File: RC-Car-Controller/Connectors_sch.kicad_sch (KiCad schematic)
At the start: 6 parts, among them J1 MCU_IF, J3 MOTOR_IF, J4 BATT_1, J5 MISC_IF, J6 ANT_IF, J7 BATT2

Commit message: Fixed Controller PCB
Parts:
- removed J3: MOTOR_IF, symbol Connector:Conn_01x06_Pin
- removed J4: BATT_1, footprints:CONN_1805375_RSP, symbol Connector:Conn_01x02_Pin
- removed J5: MISC_IF, symbol Connector:Conn_01x06_Pin
- removed J7: BATT2, footprints:CONN_1805375_RSP, symbol Connector:Conn_01x02_Pin
- added J1, J2: XT60-M, symbol XT60-M:XT60-M
- renumbered J1 to J5
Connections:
- net GND_BATT: now also J1.N (NEG), J2.N (NEG)
- net VDD_BATT: now also J1.P (POS), J2.P (POS)
- no-connect marks 7 -> 1
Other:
- note added: "Battery CON"
- moved on the sheet: J5

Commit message: Did some stuff on the Controller
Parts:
- removed J1, J2: XT60-M, symbol XT60-M:XT60-M
- added J1, J4: Conn_01x02, Connector_JST:JST_XH_B2B-XH-AM_1x02_P2.50mm_Vertical, symbol Connector_Generic:Conn_01x02
- added J2: USB_C_Receptacle_USB2.0_16P, symbol Connector:USB_C_Receptacle_USB2.0_16P
- added R18: 1Mohm, Resistor_SMD:R_0603_1608Metric, symbol Device:R
- added R19, R20: 5.11kohm, Resistor_SMD:R_0603_1608Metric, symbol Device:R
- added U2: USBLC6-2SC6, Package_TO_SOT_SMD:SOT-23-6, symbol Power_Protection:USBLC6-2SC6
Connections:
- net GND_BATT: now also J1.2 (Pin_2)
- net VDD_BATT: now also J1.1 (Pin_1), J4.2 (Pin_2)
- new net: J2.A6 (D+), J2.B6 (D+), U2.1 (I/O1)
- new net: J2.A7 (D-), J2.B7 (D-), U2.3 (I/O2)
- new net: J2.A5 (CC1), R19.2
- new net: J2.S1 (SHIELD), R18.1
- new net: J2.B5 (CC2), R20.2
- new net CON_USB_D+: U2.6 (I/O1)
- new net CON_USB_D-: U2.4 (I/O2)
- new net GND_USB: J2.A1 (GND), J2.A12 (GND), J2.B1 (GND), J2.B12 (GND), R18.2, R19.1, R20.1, U2.2 (GND)
- new net VDD_BATT_PRE_SW: J4.1 (Pin_1)
- new net VDD_USB: J2.A4 (VBUS), J2.A9 (VBUS), J2.B4 (VBUS), J2.B9 (VBUS), U2.5 (VBUS)
- no-connect marks 1 -> 3
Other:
- note added: "ESD Protection, 1/6 and 3/4 MAY be interchangable"
- note added: "Shield should be grounded on HOST side"
- note removed: "Need to find the right connectors + right sizes."
- moved on the sheet: J5, J6

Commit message: Fixed LiPo Charge/Monitor Circuitry
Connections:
- net VDD_BATT: no longer J4.2 (Pin_2)
- net VDD_BATT_PRE_SW renamed VDD_LOAD_PRE_SW
- new net VDD_LOAD: J4.2 (Pin_2)
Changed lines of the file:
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@@
 			)
 		)
-		(property "Value" "VDD_BATT"
+		(property "Value" "VDD_LOAD"
 			(at 72.39 151.13 0)
 			(effects
@@
 			)
 		)
-		(property "Value" "VDD_BATT_PRE_SW"
+		(property "Value" "VDD_LOAD_PRE_SW"
 			(at 72.39 138.43 0)
 			(effects

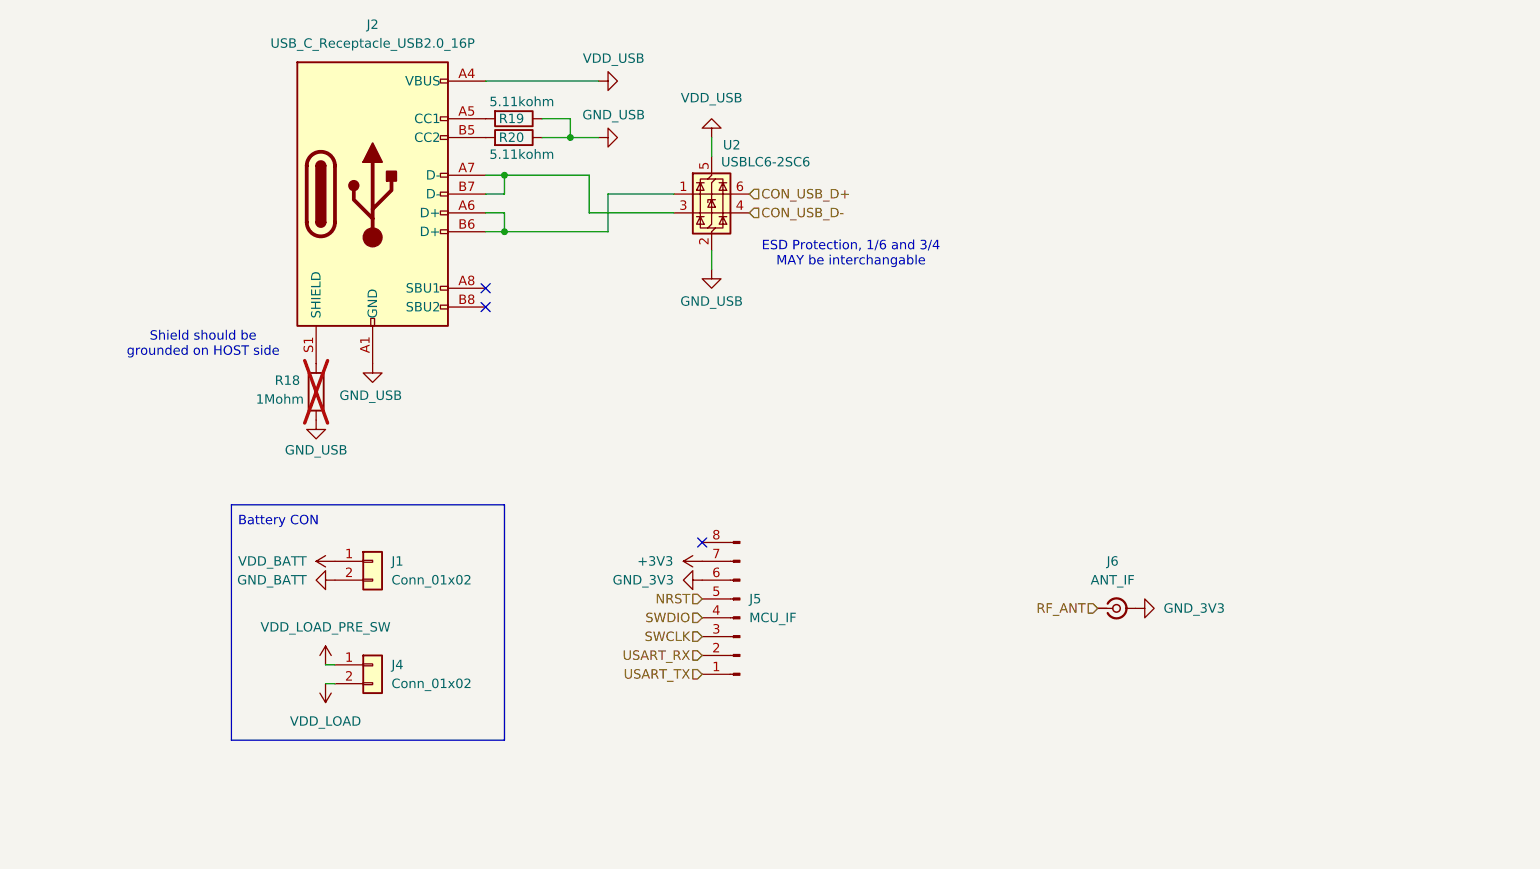
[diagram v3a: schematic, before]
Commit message: Redid USB C Footprint
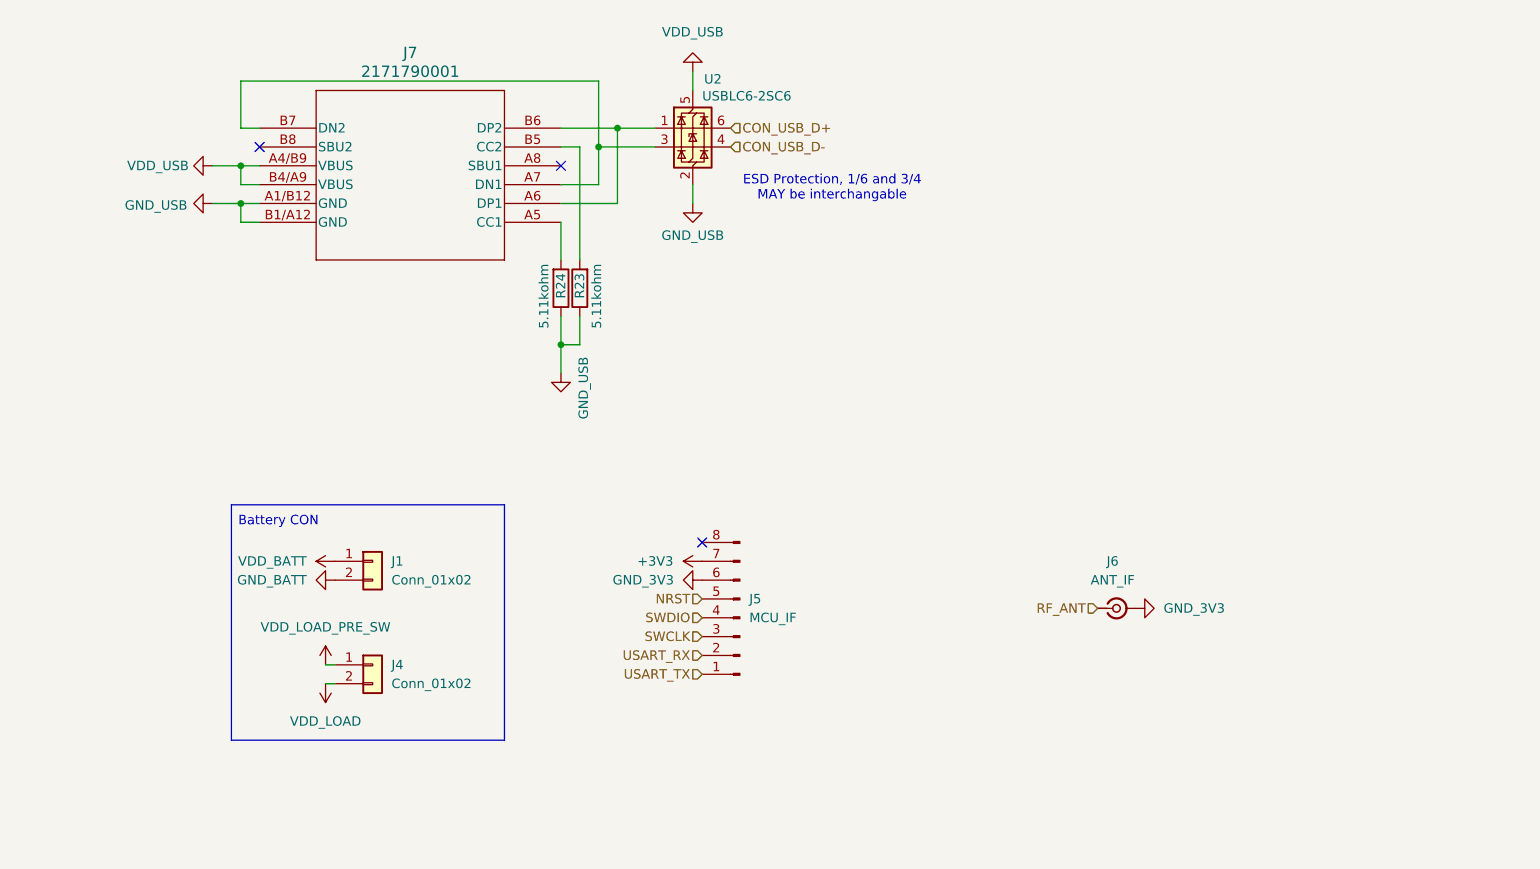
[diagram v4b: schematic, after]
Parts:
- removed J2: USB_C_Receptacle_USB2.0_16P, symbol Connector:USB_C_Receptacle_USB2.0_16P
- removed R18: 1Mohm, Resistor_SMD:R_0603_1608Metric, symbol Device:R
- removed R19, R20: 5.11kohm, Resistor_SMD:R_0603_1608Metric, symbol Device:R
- added J7: 2171790001, USB-C 2171790001:2171790001_MOL, symbol USB-C 2171790001:2171790001
- added R23, R24: 5.11kohm, Resistor_SMD:R_0603_1608Metric, symbol Device:R
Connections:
- net GND_USB: now also J7.A1/B12 (GND), J7.B1/A12 (GND), R23.1, R24.1
- net VDD_USB: now also J7.A4/B9 (VBUS), J7.B4/A9 (VBUS)
- net at U2.1 (I/O1): now also J7.A6 (DP1), J7.B6 (DP2)
- net at U2.3 (I/O2): now also J7.A7 (DN1), J7.B7 (DN2)
- new net: J7.A5 (CC1), R24.2
- new net: J7.B5 (CC2), R23.2
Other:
- note removed: "Shield should be grounded on HOST side"
- moved on the sheet: U2

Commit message: Added a switch
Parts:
- removed J4: Conn_01x02, Connector_JST:JST_XH_B2B-XH-AM_1x02_P2.50mm_Vertical, symbol Connector_Generic:Conn_01x02
- added S1: R1966ABLKBLKGR, R1966ABLKBLKGR:SW_R1966ABLKBLKGR, symbol R1966ABLKBLKGR:R1966ABLKBLKGR
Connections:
- net VDD_LOAD: now also S1.1A
- net VDD_LOAD_PRE_SW: now also S1.1
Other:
- moved on the sheet: J1
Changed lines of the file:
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@@
 		)
 	)
-	(wire
-		(pts
-			(xy 73.66 146.05) (xy 72.39 146.05)
-		)
+	(rectangle
+		(start 41.91 121.92)
+		(end 78.74 134.62)
 		(stroke
 			(width 0)
 			(type default)
 		)
-	)
-	(wire
-		(pts
-			(xy 73.66 143.51) (xy 72.39 143.51)
-		)
-		(stroke
-			(width 0)
-			(type default)
-		)
-	)
-	(rectangle
-		(start 59.69 121.92)
-		(end 96.52 153.67)
-		(stroke
-			(width 0)
-			(type default)
-		)
 		(fill
 			(type none)
@@
 	(text "Battery CON"
 		(exclude_from_sim no)
-		(at 66.04 124.206 0)
+		(at 48.26 124.206 0)
 		(effects
 			(font
@@
 	)
 	(symbol
-		(lib_id "Connector_Generic:Conn_01x02")
-		(at 78.74 143.51 0)
-		(unit 1)
-		(exclude_from_sim no)
-		(in_bom yes)
-		(on_board yes)
-		(dnp no)
-		(fields_autoplaced yes)
-		(property "Reference" "J4"
-			(at 81.28 143.5099 0)
-			(effects
-				(font
-					(size 1.27 1.27)
-				)
-				(justify left)
-			)
-		)
-		(property "Value" "Conn_01x02"
-			(at 81.28 146.0499 0)
-			(effects
-				(font
-					(size 1.27 1.27)
-				)
-				(justify left)
-			)
-		)
-		(property "Footprint" "Connector_JST:JST_XH_B2B-XH-AM_1x02_P2.50mm_Vertical"
-			(at 78.74 143.51 0)
-			(effects
-				(font
-					(size 1.27 1.27)
-				)
-				(hide yes)
-			)
-		)
-		(property "Datasheet" "~"
-			(at 78.74 143.51 0)
-			(effects
-				(font
-					(size 1.27 1.27)
-				)
-				(hide yes)
-			)
-		)
-		(property "Description" "Generic connector, single row, 01x02, script generated (kicad-library-utils/schlib/autogen/connector/)"
-			(at 78.74 143.51 0)
-			(effects
-				(font
-					(size 1.27 1.27)
-				)
-				(hide yes)
-			)
-		)
-		(pin "1"
-		)
-		(pin "2"
-		)
-		(instances
-			(project "RC-Car-Controller"
-				(path "/ba870fd1-751d-4755-8e1a-1ea86ca9e2f6/47812da9-b622-4bda-8507-4e09448e1ff5"
-					(reference "J4")
-					(unit 1)
-				)
-			)
-		)
-	)
-	(symbol
 		(lib_id "power:GND")
 		(at 104.14 104.14 0)
@@
 	(symbol
 		(lib_id "power:+3V3")
-		(at 72.39 146.05 180)
+		(at 69.85 152.4 270)
 		(unit 1)
 		(exclude_from_sim no)
@@
 		(fields_autoplaced yes)
 		(property "Reference" "#PWR013"
-			(at 72.39 142.24 0)
+			(at 66.04 152.4 0)
 			(effects
 				(font
@@
 		)
 		(property "Value" "VDD_LOAD"
-			(at 72.39 151.13 0)
-			(effects
-				(font
-					(size 1.27 1.27)
-				)
+			(at 73.66 152.3999 90)
+			(effects
+				(font
+					(size 1.27 1.27)
+				)
+				(justify left)
 			)
 		)
 		(property "Footprint" ""
-			(at 72.39 146.05 0)
+			(at 69.85 152.4 0)
 			(effects
 				(font
@@
 		)
 		(property "Datasheet" ""
-			(at 72.39 146.05 0)
+			(at 69.85 152.4 0)
 			(effects
 				(font
@@
 		)
 		(property "Description" "Power symbol creates a global label with name \"+3V3\""
-			(at 72.39 146.05 0)
+			(at 69.85 152.4 0)
 			(effects
 				(font
@@
 	)
 	(symbol
+		(lib_id "R1966ABLKBLKGR:R1966ABLKBLKGR")
+		(at 62.23 152.4 0)
+		(unit 1)
+		(exclude_from_sim no)
+		(in_bom yes)
+		(on_board yes)
+		(dnp no)
+		(fields_autoplaced yes)
+		(property "Reference" "S1"
+			(at 62.23 144.78 0)
+			(effects
+				(font
+					(size 1.27 1.27)
+				)
+			)
+		)
+		(property "Value" "R1966ABLKBLKGR"
+			(at 62.23 147.32 0)
+			(effects
+				(font
+					(size 1.27 1.27)
+				)
+			)
+		)
+		(property "Footprint" "R1966ABLKBLKGR:SW_R1966ABLKBLKGR"
+			(at 62.23 152.4 0)
+			(effects
+				(font
+					(size 1.27 1.27)
+				)
+				(justify bottom)
+				(hide yes)
+			)
+		)
+		(property "Datasheet" "https://www.digikey.com/en/products/detail/e-switch/R1966ABLKBLKGR/379042"
+			(at 62.23 152.4 0)
+			(effects
+				(font
+					(size 1.27 1.27)
+				)
+				(hide yes)
+			)
+		)
+		(property "Description" ""
+			(at 62.23 152.4 0)
+			(effects
+				(font
+					(size 1.27 1.27)
+				)
+				(hide yes)
+			)
+		)
+		(property "PARTREV" "E"
+			(at 62.23 152.4 0)
+			(effects
+				(font
+					(size 1.27 1.27)
+				)
+				(justify bottom)
+				(hide yes)
+			)
+		)
+		(property "SNAPEDA_PN" "R1966ABLKBLKGR"
+			(at 62.23 152.4 0)
+			(effects
+				(font
+					(size 1.27 1.27)
+				)
+				(justify bottom)
+				(hide yes)
+			)
+		)
+		(property "STANDARD" "Manufacturer Recommendations"
+			(at 62.23 152.4 0)
+			(effects
+				(font
+					(size 1.27 1.27)
+				)
+				(justify bottom)
+				(hide yes)
+			)
+		)
+		(property "MAXIMUM_PACKAGE_HEIGHT" "14.8 mm"
+			(at 62.23 152.4 0)
+			(effects
+				(font
+					(size 1.27 1.27)
+				)
+				(justify bottom)
+				(hide yes)
+			)
+		)
+		(property "MANUFACTURER" "E-Switch"
+			(at 62.23 152.4 0)
+			(effects
+				(font
+					(size 1.27 1.27)
+				)
+				(justify bottom)
+				(hide yes)
+			)
+		)
+		(pin "1"
+		)
+		(pin "1A"
+		)
+		(instances
+			(project ""
+				(path "/ba870fd1-751d-4755-8e1a-1ea86ca9e2f6/47812da9-b622-4bda-8507-4e09448e1ff5"
+					(reference "S1")
+					(unit 1)
+				)
+			)
+		)
+	)
+	(symbol
 		(lib_id "power:GND")
 		(at 121.92 81.28 0)
@@
 	(symbol
 		(lib_id "power:+3V3")
-		(at 72.39 143.51 0)
+		(at 54.61 152.4 90)
 		(unit 1)
 		(exclude_from_sim no)
@@
 		(fields_autoplaced yes)
 		(property "Reference" "#PWR096"
-			(at 72.39 147.32 0)
+			(at 58.42 152.4 0)
 			(effects
 				(font
@@
 		)
 		(property "Value" "VDD_LOAD_PRE_SW"
-			(at 72.39 138.43 0)
-			(effects
-				(font
-					(size 1.27 1.27)
-				)
+			(at 50.8 152.3999 90)
+			(effects
+				(font
+					(size 1.27 1.27)
+				)
+				(justify left)
 			)
 		)
 		(property "Footprint" ""
-			(at 72.39 143.51 0)
+			(at 54.61 152.4 0)
 			(effects
 				(font
@@
 		)
 		(property "Datasheet" ""
-			(at 72.39 143.51 0)
+			(at 54.61 152.4 0)
 			(effects
 				(font
@@
 		)
 		(property "Description" "Power symbol creates a global label with name \"+3V3\""
-			(at 72.39 143.51 0)
+			(at 54.61 152.4 0)
 			(effects
 				(font
@@
 	(symbol
 		(lib_id "Connector_Generic:Conn_01x02")
-		(at 78.74 129.54 0)
+		(at 60.96 129.54 0)
 		(unit 1)
 		(exclude_from_sim no)
@@
 		(fields_autoplaced yes)
 		(property "Reference" "J1"
-			(at 81.28 129.5399 0)
+			(at 63.5 129.5399 0)
 			(effects
 				(font
@@
 		)
 		(property "Value" "Conn_01x02"
-			(at 81.28 132.0799 0)
+			(at 63.5 132.0799 0)
 			(effects
 				(font
@@
 		)
 		(property "Footprint" "Connector_JST:JST_XH_B2B-XH-AM_1x02_P2.50mm_Vertical"
-			(at 78.74 129.54 0)
+			(at 60.96 129.54 0)
 			(effects
 				(font
@@
 		)
 		(property "Datasheet" "~"
-			(at 78.74 129.54 0)
+			(at 60.96 129.54 0)
 			(effects
 				(font
@@
 		)
 		(property "Description" "Generic connector, single row, 01x02, script generated (kicad-library-utils/schlib/autogen/connector/)"
-			(at 78.74 129.54 0)
+			(at 60.96 129.54 0)
 			(effects
 				(font
@@
 	(symbol
 		(lib_id "power:+3V3")
-		(at 73.66 129.54 90)
+		(at 55.88 129.54 90)
 		(unit 1)
 		(exclude_from_sim no)
@@
 		(fields_autoplaced yes)
 		(property "Reference" "#PWR092"
-			(at 77.47 129.54 0)
+			(at 59.69 129.54 0)
 			(effects
 				(font
@@
 		)
 		(property "Value" "VDD_BATT"
-			(at 69.85 129.5399 90)
+			(at 52.07 129.5399 90)
 			(effects
 				(font
@@
 		)
 		(property "Footprint" ""
-			(at 73.66 129.54 0)
+			(at 55.88 129.54 0)
 			(effects
 				(font
@@
 		)
 		(property "Datasheet" ""
-			(at 73.66 129.54 0)
+			(at 55.88 129.54 0)
 			(effects
 				(font
@@
 		)
 		(property "Description" "Power symbol creates a global label with name \"+3V3\""
-			(at 73.66 129.54 0)
+			(at 55.88 129.54 0)
 			(effects
 				(font
@@
 	(symbol
 		(lib_id "power:GND")
-		(at 73.66 132.08 270)
+		(at 55.88 132.08 270)
 		(unit 1)
 		(exclude_from_sim no)
@@
 		(fields_autoplaced yes)
 		(property "Reference" "#PWR093"
-			(at 67.31 132.08 0)
+			(at 49.53 132.08 0)
 			(effects
 				(font
@@
 		)
 		(property "Value" "GND_BATT"
-			(at 69.85 132.0799 90)
+			(at 52.07 132.0799 90)
 			(effects
 				(font
@@
 		)
 		(property "Footprint" ""
-			(at 73.66 132.08 0)
+			(at 55.88 132.08 0)
 			(effects
 				(font
@@
 		)
 		(property "Datasheet" ""
-			(at 73.66 132.08 0)
+			(at 55.88 132.08 0)
 			(effects
 				(font
@@
 		)
 		(property "Description" "Power symbol creates a global label with name \"GND\" , ground"
-			(at 73.66 132.08 0)
-			(effects
-				(font
+			(at 55.88 132.08 0)
+			(effects
+				(font

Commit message: Did power schtuff
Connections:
- net CON_USB_D+: now also U2.4 (I/O2); no longer U2.6 (I/O1)
- net CON_USB_D-: now also U2.6 (I/O1); no longer U2.4 (I/O2)
- net at J7.A6 (DP1), J7.B6 (DP2): now also U2.3 (I/O2); no longer U2.1 (I/O1)
- net at J7.A7 (DN1), J7.B7 (DN2): now also U2.1 (I/O1); no longer U2.3 (I/O2)
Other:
- moved on the sheet: U2
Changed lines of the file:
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@@
 	(paper "A4")
 	(junction
-		(at 111.76 71.12)
+		(at 111.76 81.28)
 		(diameter 0)
 		(color 0 0 0 0)
@@
 	)
 	(junction
-		(at 109.22 73.66)
+		(at 109.22 78.74)
 		(diameter 0)
 		(color 0 0 0 0)
@@
 	(wire
 		(pts
-			(xy 111.76 71.12) (xy 116.84 71.12)
-		)
-		(stroke
-			(width 0)
-			(type default)
-		)
-	)
-	(wire
-		(pts
 			(xy 104.14 83.82) (xy 104.14 88.9)
 		)
@@
 	(wire
 		(pts
-			(xy 109.22 78.74) (xy 109.22 73.66)
+			(xy 109.22 64.77) (xy 109.22 78.74)
 		)
 		(stroke
@@
 	(wire
 		(pts
-			(xy 109.22 73.66) (xy 116.84 73.66)
-		)
-		(stroke
-			(width 0)
-			(type default)
-		)
-	)
-	(wire
-		(pts
 			(xy 60.96 81.28) (xy 63.5 81.28)
 		)
@@
 	(wire
 		(pts
-			(xy 109.22 73.66) (xy 109.22 64.77)
-		)
-		(stroke
-			(width 0)
-			(type default)
-		)
-	)
-	(wire
-		(pts
 			(xy 104.14 78.74) (xy 109.22 78.74)
 		)
@@
 	(wire
 		(pts
-			(xy 121.92 63.5) (xy 121.92 66.04)
-		)
-		(stroke
-			(width 0)
-			(type default)
-		)
-	)
-	(wire
-		(pts
-			(xy 121.92 81.28) (xy 121.92 78.74)
+			(xy 121.92 71.12) (xy 121.92 73.66)
+		)
+		(stroke
+			(width 0)
+			(type default)
+		)
+	)
+	(wire
+		(pts
+			(xy 121.92 88.9) (xy 121.92 86.36)
+		)
+		(stroke
+			(width 0)
+			(type default)
+		)
+	)
+	(wire
+		(pts
+			(xy 111.76 81.28) (xy 116.84 81.28)
 		)
 		(stroke
@@
 		(pts
 			(xy 60.96 71.12) (xy 63.5 71.12)
+		)
+		(stroke
+			(width 0)
+			(type default)
+		)
+	)
+	(wire
+		(pts
+			(xy 109.22 78.74) (xy 116.84 78.74)
 		)
 		(stroke
@@
 	(text "ESD Protection, 1/6 and 3/4 \nMAY be interchangable"
 		(exclude_from_sim no)
-		(at 140.716 79.248 0)
+		(at 140.716 86.868 0)
 		(effects
 			(font
@@
 	(hierarchical_label "CON_USB_D-"
 		(shape input)
-		(at 127 73.66 0)
+		(at 127 78.74 0)
 		(fields_autoplaced yes)
 		(effects
@@
 	(hierarchical_label "CON_USB_D+"
 		(shape input)
-		(at 127 71.12 0)
+		(at 127 81.28 0)
 		(fields_autoplaced yes)
 		(effects
@@
 	(symbol
 		(lib_id "Power_Protection:USBLC6-2SC6")
-		(at 121.92 71.12 0)
+		(at 121.92 78.74 0)
 		(unit 1)
 		(exclude_from_sim no)
@@
 		(dnp no)
 		(property "Reference" "U2"
-			(at 123.444 64.516 0)
+			(at 123.444 72.136 0)
 			(effects
 				(font
@@
 		)
 		(property "Value" "USBLC6-2SC6"
-			(at 123.19 66.802 0)
+			(at 123.19 74.422 0)
 			(effects
 				(font
@@
 		)
 		(property "Footprint" "Package_TO_SOT_SMD:SOT-23-6"
-			(at 123.19 77.47 0)
+			(at 123.19 85.09 0)
 			(effects
 				(font
@@
 		)
 		(property "Datasheet" "https://www.digikey.ca/en/products/detail/stmicroelectronics/USBLC6-2SC6/1040559"
-			(at 123.19 79.375 0)
+			(at 123.19 86.995 0)
 			(effects
 				(font
@@
 		)
 		(property "Description" "Very low capacitance ESD protection diode, 2 data-line, SOT-23-6"
-			(at 121.92 71.12 0)
+			(at 121.92 78.74 0)
 			(effects
 				(font
@@
 	(symbol
 		(lib_id "power:GND")
-		(at 121.92 81.28 0)
+		(at 121.92 88.9 0)
 		(unit 1)
 		(exclude_from_sim no)
@@
 		(dnp no)
 		(property "Reference" "#PWR043"
-			(at 121.92 87.63 0)
+			(at 121.92 95.25 0)
 			(effects
 				(font
@@
 		)
 		(property "Value" "GND_USB"
-			(at 121.92 85.598 0)
+			(at 121.92 93.218 0)
 			(effects
 				(font
@@
 		)
 		(property "Footprint" ""
-			(at 121.92 81.28 0)
+			(at 121.92 88.9 0)
 			(effects
 				(font
@@
 		)
 		(property "Datasheet" ""
-			(at 121.92 81.28 0)
+			(at 121.92 88.9 0)
 			(effects
 				(font
@@
 		)
 		(property "Description" "Power symbol creates a global label with name \"GND\" , ground"
-			(at 121.92 81.28 0)
+			(at 121.92 88.9 0)
 			(effects
 				(font
@@
 	(symbol
 		(lib_id "power:GND")
-		(at 121.92 63.5 180)
+		(at 121.92 71.12 180)
 		(unit 1)
 		(exclude_from_sim no)
@@
 		(dnp no)
 		(property "Reference" "#PWR042"
-			(at 121.92 57.15 0)
+			(at 121.92 64.77 0)
 			(effects
 				(font
@@
 		)
 		(property "Value" "VDD_USB"
-			(at 121.92 58.166 0)
+			(at 121.92 65.786 0)
 			(effects
 				(font
@@
 		)
 		(property "Footprint" ""
-			(at 121.92 63.5 0)
+			(at 121.92 71.12 0)
 			(effects
 				(font
@@
 		)
 		(property "Datasheet" ""
-			(at 121.92 63.5 0)
+			(at 121.92 71.12 0)
 			(effects
 				(font
@@
 		)
 		(property "Description" "Power symbol creates a global label with name \"GND\" , ground"
-			(at 121.92 63.5 0)
-			(effects
-				(font
+			(at 121.92 71.12 0)
+			(effects
+				(font
